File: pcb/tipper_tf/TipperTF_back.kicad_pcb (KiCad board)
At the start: 2 copper layers, 238.3 x 110.3 mm, 8 parts

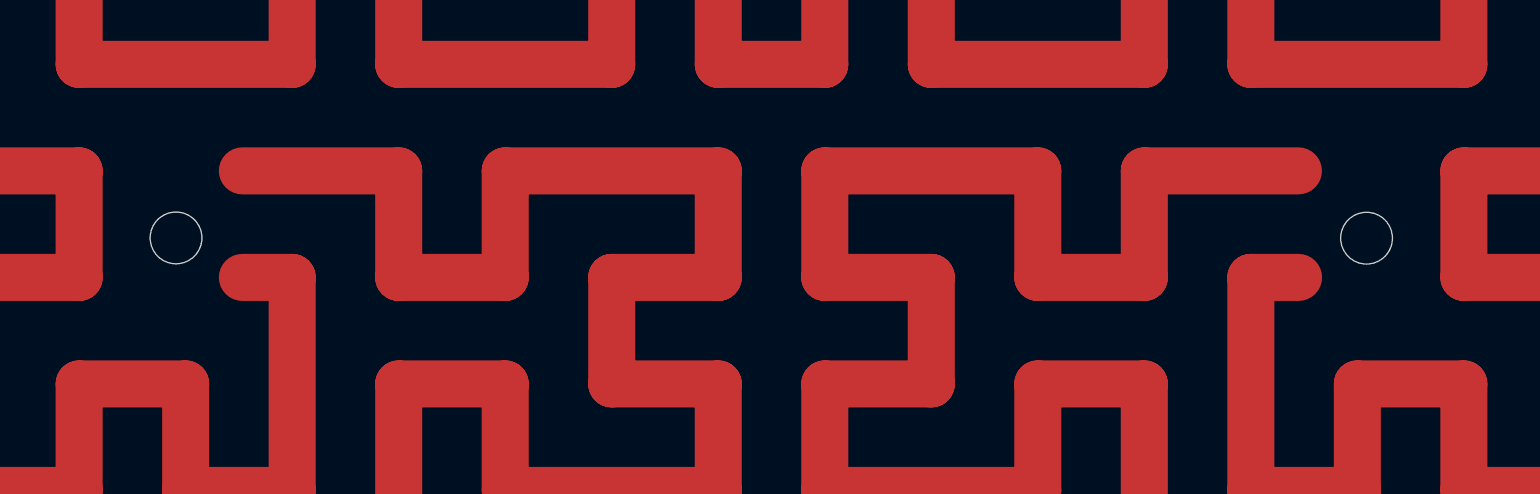
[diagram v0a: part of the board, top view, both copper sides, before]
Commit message: change: spacer and backside pcbs changed to reflect changes in case and main pcb
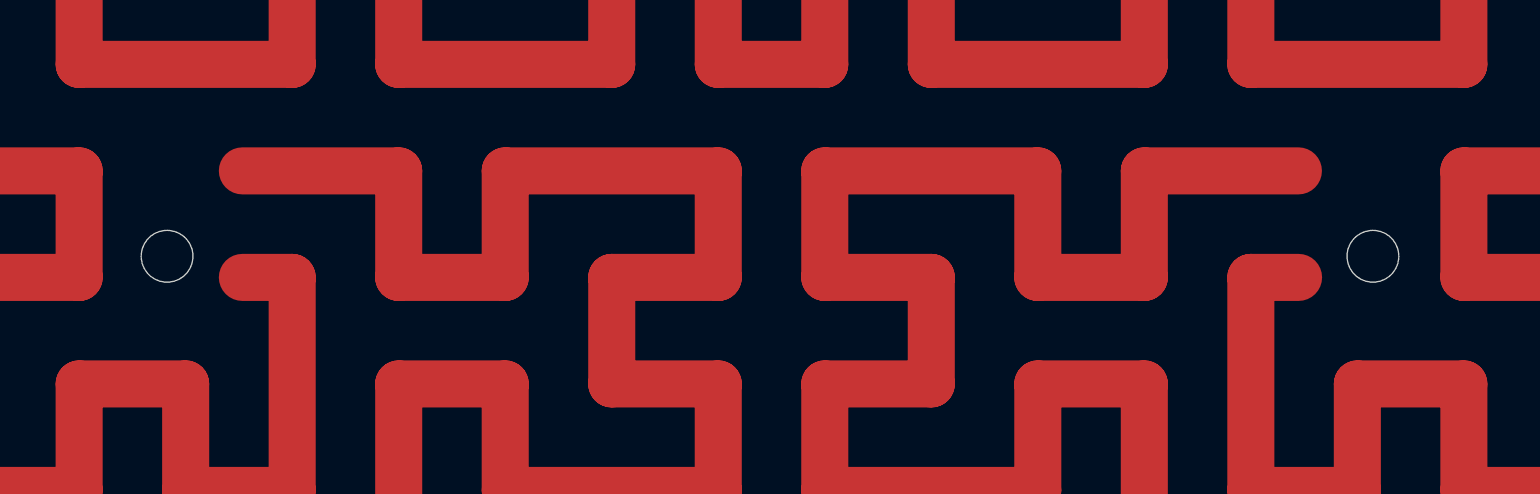
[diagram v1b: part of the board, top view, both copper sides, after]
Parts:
- moved REF** 0.87 mm to (127.7, 123.4)
- moved REF** 0.82 mm to (178.9, 123.4)
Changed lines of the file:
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@@
-(kicad_pcb (version 20210824) (generator pcbnew)
+(kicad_pcb (version 20210925) (generator pcbnew)
   (general
     (thickness 1.2)
@@
   (net 0 "")
   (footprint "MountingHole:MountingHole_2.2mm_M2_DIN965" (layer "F.Cu")
-    (at 178.65 122.64)
+    (at 178.92 123.41)
     (descr "Mounting Hole 2.2mm, no annular, M2, DIN965")
     (tags "mounting hole 2.2mm no annular m2 din965")
@@
   )
   (footprint "MountingHole:MountingHole_2.2mm_M2_DIN965" (layer "F.Cu")
-    (at 128.06 122.63)
+    (at 127.68 123.41)
     (descr "Mounting Hole 2.2mm, no annular, M2, DIN965")
     (tags "mounting hole 2.2mm no annular m2 din965")
